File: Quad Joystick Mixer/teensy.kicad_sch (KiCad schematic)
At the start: 11 parts, among them U20 Teensy4.0

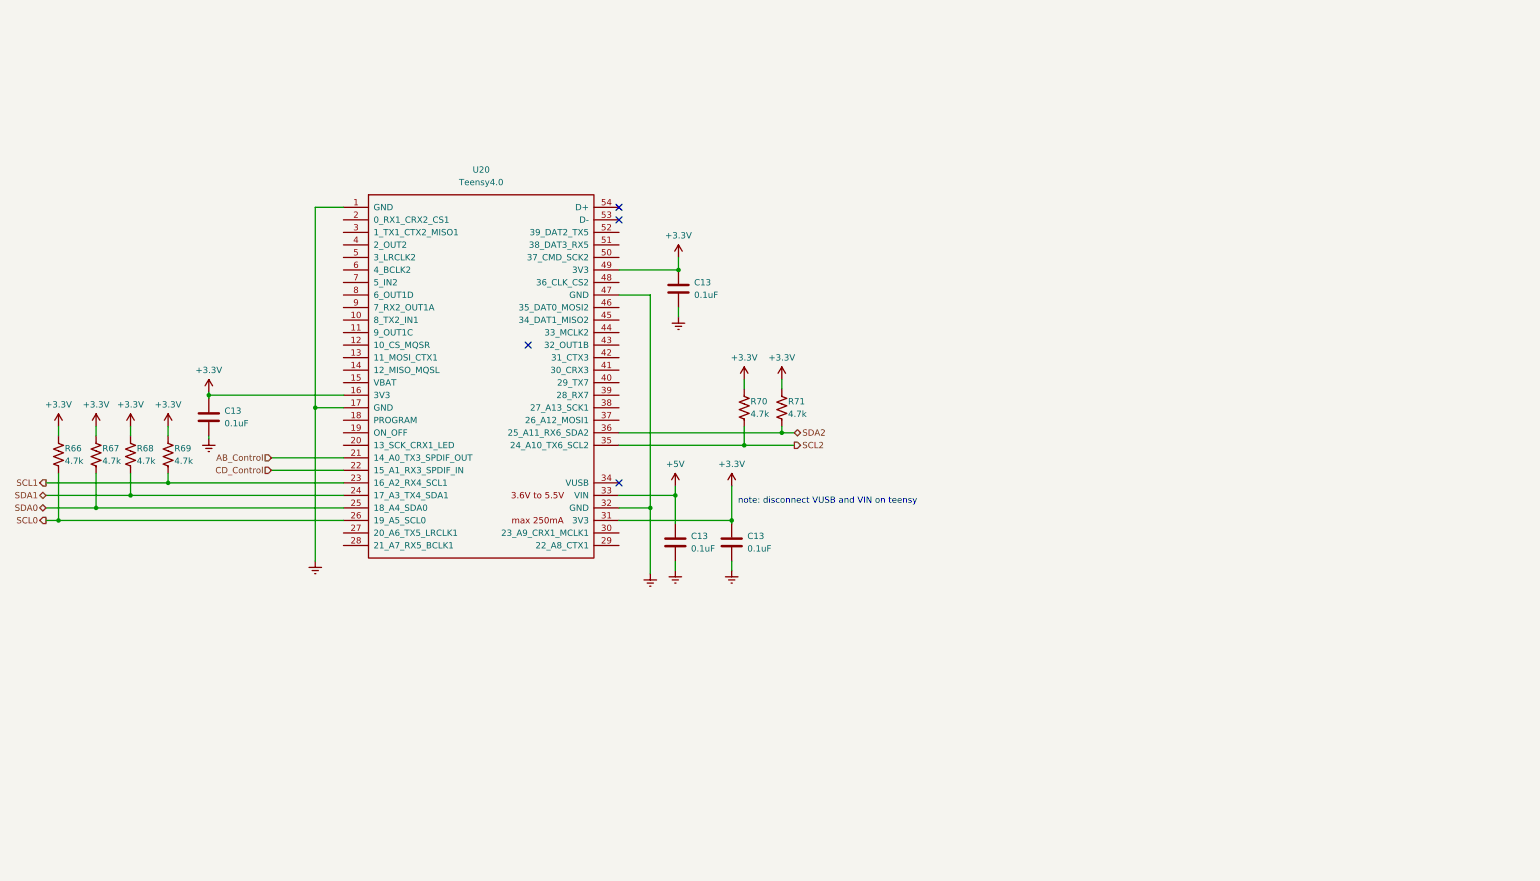
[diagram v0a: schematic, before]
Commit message: add in rotary circuit and some docs
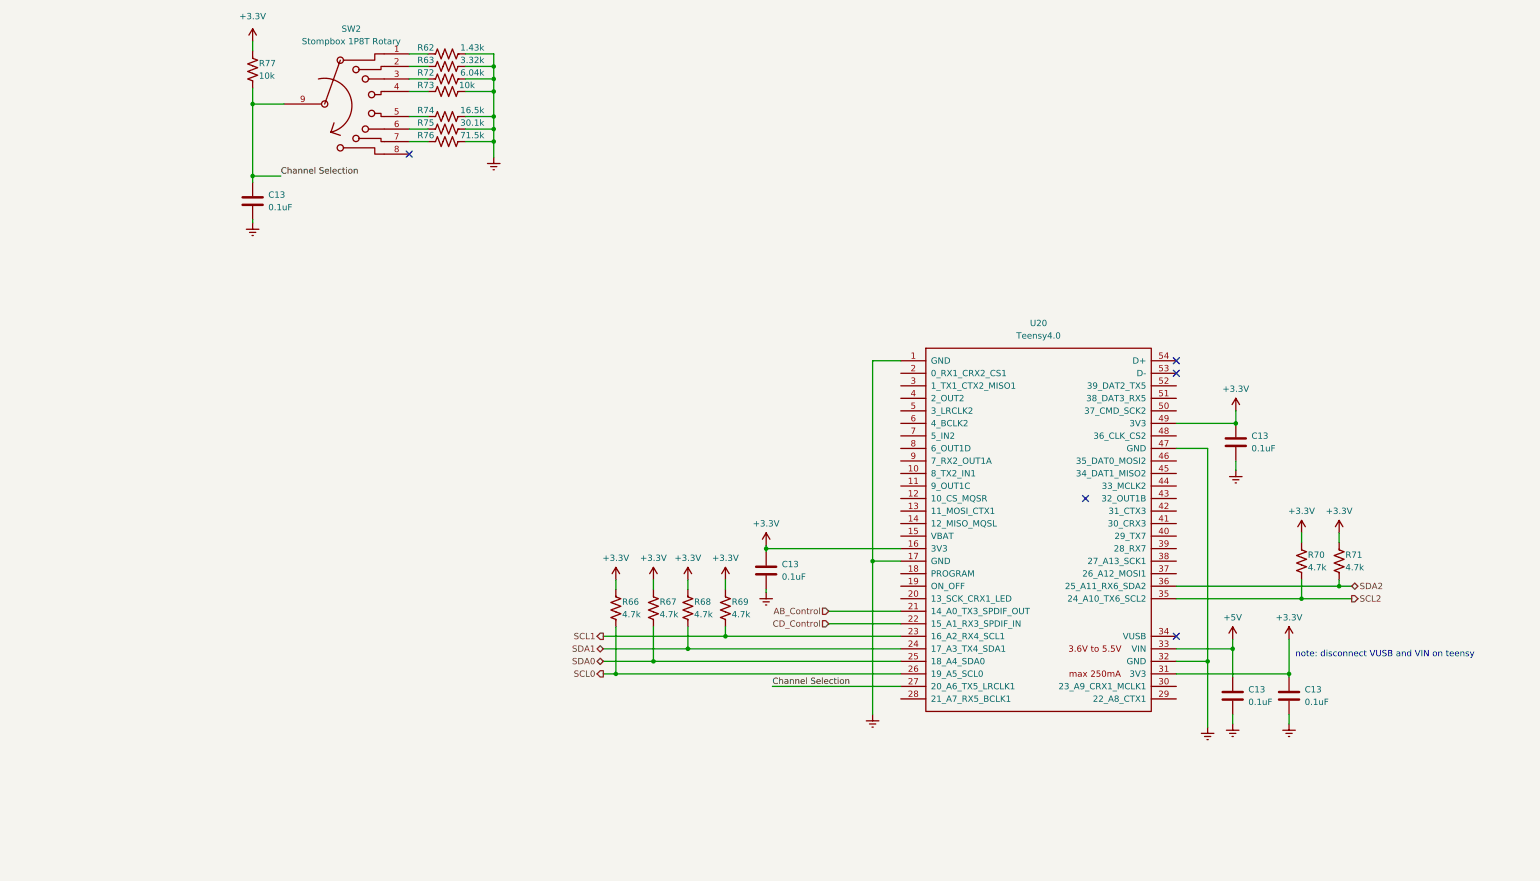
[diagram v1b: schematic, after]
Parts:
- added C13: 0.1uF, Capacitor_SMD:C_0805_2012Metric_Pad1.18x1.45mm_HandSolder, symbol Device:C
- added R62: 1.43k, symbol Device:R_US
- added R63: 3.32k, symbol Device:R_US
- added R72: 6.04k, symbol Device:R_US
- added R73, R77: 10k, symbol Device:R_US
- added R74: 16.5k, symbol Device:R_US
- added R75: 30.1k, symbol Device:R_US
- added R76: 71.5k, symbol Device:R_US
- added SW2: Stompbox 1P8T Rotary, Eyewool Switches:Stompbox 1P8T Rotary, symbol Eyewool_Switches:Stompbox 1P8T Rotary
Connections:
- net +3.3V: now also R77.1
- net Earth: now also C13.2, R62.2, R63.2, R72.2, R73.2, R74.2, R75.2, R76.2
- net Channel Selection: now reaches U20.27 (20_A6_TX5_LRCLK1)
- net Channel Selection: now also C13.1, R77.2, SW2.9
- new net: R63.1, SW2.2
- new net: R72.1, SW2.3
- new net: R62.1, SW2.1
- new net: R73.1, SW2.4
- new net: R74.1, SW2.5
- new net: R75.1, SW2.6
- new net: R76.1, SW2.7
- no-connect marks 4 -> 5
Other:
- moved on the sheet: C13, R66, R67, R68, R69, R70, R71, U20

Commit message: finished first draft of the schematic
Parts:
- removed C13: 0.1uF, Capacitor_SMD:C_0805_2012Metric_Pad1.18x1.45mm_HandSolder, symbol Device:C
- removed R62: 1.43k, symbol Device:R_US
- removed R63: 3.32k, symbol Device:R_US
- removed R72: 6.04k, symbol Device:R_US
- removed R73, R77: 10k, symbol Device:R_US
- removed R74: 16.5k, symbol Device:R_US
- removed R75: 30.1k, symbol Device:R_US
- removed R76: 71.5k, symbol Device:R_US
- removed SW2: Stompbox 1P8T Rotary, Eyewool Switches:Stompbox 1P8T Rotary, symbol Eyewool_Switches:Stompbox 1P8T Rotary
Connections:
- net Button_3: now reaches U20.10 (8_TX2_IN1)
- net LED_1: now reaches U20.4 (2_OUT2)
- net LED_2: now reaches U20.5 (3_LRCLK2)
- net Button_1: now reaches U20.8 (6_OUT1D)
- net Button_2: now reaches U20.9 (7_RX2_OUT1A)
- no-connect marks 5 -> 4
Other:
- note added: "Microcontroller"
- title: (none) -> Quadrophonic Joystick Mixer
- moved on the sheet: C13, R66, R67, R68, R69, R70, R71, U20

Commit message: ok the draft wasn't done but now i think it is
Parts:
- added C13 (x2): 0.1uF, Capacitor_SMD:C_0805_2012Metric_Pad1.18x1.45mm_HandSolder, symbol Device:C
- added D24 (x2): SMAJ3.3A, Diode_SMD:D_SMA, symbol Diode:SMAJ5.0A
- added SW5 (x2): ~, symbol Switch:SW_SPST
- added TP1: TestPoint, TestPoint:TestPoint_THTPad_D1.5mm_Drill0.7mm, symbol Connector:TestPoint
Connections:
- net +3.3V: now also TP1.1
- net Earth: now also C13.2, C13.2, D24.2 (A2), D24.2 (A2), SW5.2 (B), SW5.2 (B)
- net PROGRAM: now reaches U20.18 (PROGRAM)
- net PROGRAM: now also C13.1, D24.1 (A1), SW5.1 (A)
- net POWER: now reaches U20.19 (ON_OFF)
- net POWER: now also C13.1, D24.1 (A1), SW5.1 (A)
- no-connect marks 4 -> 29

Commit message: clean up after review, working through BOM
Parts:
- D24: value SMAJ3.3A -> SMAJ5.0A; DK PN (none) -> SMAJ5.0A-FDICT-ND; MPN (none) -> SMAJ5.0A-13-F
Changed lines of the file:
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@@
       (effects (font (size 1.27 1.27)) (justify left))
     )
-    (property "Value" "SMAJ3.3A" (at 199.39 191.135 90)
+    (property "Value" "SMAJ5.0A" (at 199.39 191.135 90)
       (effects (font (size 1.27 1.27)) (justify left))
     )
@@
     )
     (property "Datasheet" "https://www.littelfuse.com/media?resourcetype=datasheets&itemid=75e32973-b177-4ee3-a0ff-cedaf1abdb93&filename=smaj-datasheet" (at 196.85 188.595 0)
+      (effects (font (size 1.27 1.27)) hide)
+    )
+    (property "DK PN" "SMAJ5.0A-FDICT-ND" (at 196.85 189.865 0)
+      (effects (font (size 1.27 1.27)) hide)
+    )
+    (property "MPN" "SMAJ5.0A-13-F" (at 196.85 189.865 0)
       (effects (font (size 1.27 1.27)) hide)
     )
@@
       (effects (font (size 1.27 1.27)) (justify left))
     )
-    (property "Value" "SMAJ3.3A" (at 144.145 187.96 90)
+    (property "Value" "SMAJ5.0A" (at 144.145 187.96 90)
       (effects (font (size 1.27 1.27)) (justify left))
     )
@@
       (effects (font (size 1.27 1.27)) hide)
     )
+    (property "DK PN" "SMAJ5.0A-FDICT-ND" (at 141.605 186.69 0)
+      (effects (font (size 1.27 1.27)) hide)
+    )
+    (property "MPN" "SMAJ5.0A-13-F" (at 141.605 186.69 0)
+      (effects (font (size 1.27 1.27)) hide)
+    )

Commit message: finish adding parts to the BOM
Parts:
- C13, D24: Source (none) -> DK
- R66, R67, R68, R69, R70, R71: footprint (none) -> Resistor_SMD:R_0805_2012Metric_Pad1.20x1.40mm_HandSolder; DK PN (none) -> RMCF0805JT4K70CT-ND; MPN (none) -> RMCF0805JT4K70; Source (none) -> DK
- SW5: value ~ -> Cherry MX; footprint (none) -> Button_Switch_Keyboard:SW_Cherry_MX_1.00u_PCB; DK PN (none) -> CH160-ND; MPN (none) -> MX1A-11NW; Source (none) -> DK
- TP1: Source (none) -> NA
- U20: Source (none) -> Teensy
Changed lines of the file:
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@@
+      (effects (font (size 1.27 1.27)) hide)
+    )
+    (property "Source" "DK" (at 128.905 185.42 0)
       (effects (font (size 1.27 1.27)) hide)
     )
@@
     )
     (property "MPN" "CL21B104KBCNNNC" (at 248.92 114.935 0)
+      (effects (font (size 1.27 1.27)) hide)
+    )
+    (property "Source" "DK" (at 248.92 114.935 0)
       (effects (font (size 1.27 1.27)) hide)
     )
@@
       (effects (font (size 1.27 1.27)) hide)
     )
+    (property "Source" "DK" (at 259.715 166.37 0)
+      (effects (font (size 1.27 1.27)) hide)
+    )
     (pin "1")
     (pin "2")
@@
       (effects (font (size 1.27 1.27)) (justify left))
     )
-    (property "Footprint" "" (at 124.206 148.844 90)
+    (property "Footprint" "Resistor_SMD:R_0805_2012Metric_Pad1.20x1.40mm_HandSolder" (at 124.206 148.844 90)
       (effects (font (size 1.27 1.27)) hide)
     )
@@
       (effects (font (size 1.27 1.27)) hide)
     )
+    (property "Source" "DK" (at 123.19 148.59 0)
+      (effects (font (size 1.27 1.27)) hide)
+    )
+    (property "DK PN" "RMCF0805JT4K70CT-ND" (at 123.19 148.59 0)
+      (effects (font (size 1.27 1.27)) hide)
+    )
+    (property "MPN" "RMCF0805JT4K70" (at 123.19 148.59 0)
+      (effects (font (size 1.27 1.27)) hide)
+    )
     (pin "1")
     (pin "2")
@@
     )
     (property "MPN" "CL21B104KBCNNNC" (at 248.285 166.37 0)
+      (effects (font (size 1.27 1.27)) hide)
+    )
+    (property "Source" "DK" (at 248.285 166.37 0)
       (effects (font (size 1.27 1.27)) hide)
     )
@@
       (effects (font (size 1.27 1.27)) (justify left))
     )
-    (property "Footprint" "" (at 270.891 139.319 90)
+    (property "Footprint" "Resistor_SMD:R_0805_2012Metric_Pad1.20x1.40mm_HandSolder" (at 270.891 139.319 90)
       (effects (font (size 1.27 1.27)) hide)
     )
     (property "Datasheet" "~" (at 269.875 139.065 0)
+      (effects (font (size 1.27 1.27)) hide)
+    )
+    (property "Source" "DK" (at 269.875 139.065 0)
+      (effects (font (size 1.27 1.27)) hide)
+    )
+    (property "DK PN" "RMCF0805JT4K70CT-ND" (at 269.875 139.065 0)
+      (effects (font (size 1.27 1.27)) hide)
+    )
+    (property "MPN" "RMCF0805JT4K70" (at 269.875 139.065 0)
       (effects (font (size 1.27 1.27)) hide)
     )
@@
     )
     (property "Datasheet" "~" (at 266.7 165.1 0)
+      (effects (font (size 1.27 1.27)) hide)
+    )
+    (property "Source" "NA" (at 266.7 160.02 0)
       (effects (font (size 1.27 1.27)) hide)
     )
@@
       (effects (font (size 1.27 1.27)) (justify left))
     )
-    (property "Footprint" "" (at 138.811 148.844 90)
+    (property "Footprint" "Resistor_SMD:R_0805_2012Metric_Pad1.20x1.40mm_HandSolder" (at 138.811 148.844 90)
       (effects (font (size 1.27 1.27)) hide)
     )
@@
       (effects (font (size 1.27 1.27)) hide)
     )
+    (property "Source" "DK" (at 137.795 148.59 0)
+      (effects (font (size 1.27 1.27)) hide)
+    )
+    (property "DK PN" "RMCF0805JT4K70CT-ND" (at 137.795 148.59 0)
+      (effects (font (size 1.27 1.27)) hide)
+    )
+    (property "MPN" "RMCF0805JT4K70" (at 137.795 148.59 0)
+      (effects (font (size 1.27 1.27)) hide)
+    )
     (pin "1")
     (pin "2")
@@
     )
     (property "MPN" "CL21B104KBCNNNC" (at 153.67 140.97 0)
+      (effects (font (size 1.27 1.27)) hide)
+    )
+    (property "Source" "DK" (at 153.67 140.97 0)
       (effects (font (size 1.27 1.27)) hide)
     )
@@
       (effects (font (size 1.27 1.27)) (justify left))
     )
-    (property "Footprint" "" (at 146.431 148.844 90)
+    (property "Footprint" "Resistor_SMD:R_0805_2012Metric_Pad1.20x1.40mm_HandSolder" (at 146.431 148.844 90)
       (effects (font (size 1.27 1.27)) hide)
     )
     (property "Datasheet" "~" (at 145.415 148.59 0)
+      (effects (font (size 1.27 1.27)) hide)
+    )
+    (property "Source" "DK" (at 145.415 148.59 0)
+      (effects (font (size 1.27 1.27)) hide)
+    )
+    (property "DK PN" "RMCF0805JT4K70CT-ND" (at 145.415 148.59 0)
+      (effects (font (size 1.27 1.27)) hide)
+    )
+    (property "MPN" "RMCF0805JT4K70" (at 145.415 148.59 0)
       (effects (font (size 1.27 1.27)) hide)
     )
@@
       (effects (font (size 1.27 1.27)) (justify left))
     )
-    (property "Value" "~" (at 160.02 187.325 90)
-      (effects (font (size 1.27 1.27)) (justify left))
-    )
-    (property "Footprint" "" (at 157.48 186.055 0)
+    (property "Value" "Cherry MX" (at 160.02 187.325 90)
+      (effects (font (size 1.27 1.27)) (justify left))
+    )
+    (property "Footprint" "Button_Switch_Keyboard:SW_Cherry_MX_1.00u_PCB" (at 157.48 186.055 0)
       (effects (font (size 1.27 1.27)) hide)
     )
     (property "Datasheet" "~" (at 157.48 186.055 0)
+      (effects (font (size 1.27 1.27)) hide)
+    )
+    (property "Source" "DK" (at 157.48 186.055 0)
+      (effects (font (size 1.27 1.27)) hide)
+    )
+    (property "DK PN" "CH160-ND" (at 157.48 186.055 0)
+      (effects (font (size 1.27 1.27)) hide)
+    )
+    (property "MPN" "MX1A-11NW" (at 157.48 186.055 0)
       (effects (font (size 1.27 1.27)) hide)
     )
@@
     )
     (property "MPN" "CL21B104KBCNNNC" (at 184.15 188.595 0)
+      (effects (font (size 1.27 1.27)) hide)
+    )
+    (property "Source" "DK" (at 184.15 188.595 0)
       (effects (font (size 1.27 1.27)) hide)
     )
@@
       (effects (font (size 1.27 1.27)) (justify left))
     )
-    (property "Footprint" "" (at 263.271 139.319 90)
+    (property "Footprint" "Resistor_SMD:R_0805_2012Metric_Pad1.20x1.40mm_HandSolder" (at 263.271 139.319 90)
       (effects (font (size 1.27 1.27)) hide)
     )
     (property "Datasheet" "~" (at 262.255 139.065 0)
+      (effects (font (size 1.27 1.27)) hide)
+    )
+    (property "Source" "DK" (at 262.255 139.065 0)
+      (effects (font (size 1.27 1.27)) hide)
+    )
+    (property "DK PN" "RMCF0805JT4K70CT-ND" (at 262.255 139.065 0)
+      (effects (font (size 1.27 1.27)) hide)
+    )
+    (property "MPN" "RMCF0805JT4K70" (at 262.255 139.065 0)
       (effects (font (size 1.27 1.27)) hide)
     )
@@
       (effects (font (size 1.27 1.27)) hide)
     )
+    (property "Source" "DK" (at 196.85 189.865 0)
+      (effects (font (size 1.27 1.27)) hide)
+    )
     (pin "1")
     (pin "2")
@@
     )
     (property "Datasheet" "" (at 198.755 127.635 0)
+      (effects (font (size 1.27 1.27)) hide)
+    )
+    (property "Source" "Teensy" (at 208.915 132.715 0)
       (effects (font (size 1.27 1.27)) hide)
     )
@@
       (effects (font (size 1.27 1.27)) (justify left))
     )
-    (property "Value" "~" (at 215.265 190.5 90)
-      (effects (font (size 1.27 1.27)) (justify left))
-    )
-    (property "Footprint" "" (at 212.725 189.23 0)
+    (property "Value" "Cherry MX" (at 215.265 190.5 90)
+      (effects (font (size 1.27 1.27)) (justify left))
+    )
+    (property "Footprint" "Button_Switch_Keyboard:SW_Cherry_MX_1.00u_PCB" (at 212.725 189.23 0)
       (effects (font (size 1.27 1.27)) hide)
     )
     (property "Datasheet" "~" (at 212.725 189.23 0)
+      (effects (font (size 1.27 1.27)) hide)
+    )
+    (property "Source" "DK" (at 212.725 189.23 0)
+      (effects (font (size 1.27 1.27)) hide)
+    )
+    (property "DK PN" "CH160-ND" (at 212.725 189.23 0)
+      (effects (font (size 1.27 1.27)) hide)
+    )
+    (property "MPN" "MX1A-11NW" (at 212.725 189.23 0)
       (effects (font (size 1.27 1.27)) hide)
     )
@@
     )
     (property "MPN" "SMAJ5.0A-13-F" (at 141.605 186.69 0)
+      (effects (font (size 1.27 1.27)) hide)
+    )
+    (property "Source" "DK" (at 141.605 186.69 0)
       (effects (font (size 1.27 1.27)) hide)
     )
@@
       (effects (font (size 1.27 1.27)) (justify left))
     )
-    (property "Footprint" "" (at 131.826 148.844 90)
+    (property "Footprint" "Resistor_SMD:R_0805_2012Metric_Pad1.20x1.40mm_HandSolder" (at 131.826 148.844 90)
       (effects (font (size 1.27 1.27)) hide)
     )
@@
       (effects (font (size 1.27 1.27)) hide)
     )
+    (property "Source" "DK" (at 130.81 148.59 0)
+      (effects (font (size 1.27 1.27)) hide)
+    )
+    (property "DK PN" "RMCF0805JT4K70CT-ND" (at 130.81 148.59 0)
+      (effects (font (size 1.27 1.27)) hide)
+    )
+    (property "MPN" "RMCF0805JT4K70" (at 130.81 148.59 0)
+      (effects (font (size 1.27 1.27)) hide)
+    )

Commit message: work on placement and layout
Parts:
- removed C13: 0.1uF, Capacitor_SMD:C_0805_2012Metric_Pad1.18x1.45mm_HandSolder, symbol Device:C
- removed R70, R71: 4.7k, Resistor_SMD:R_0805_2012Metric_Pad1.20x1.40mm_HandSolder, symbol Device:R_US
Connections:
- net +3.3V: no longer U20.49 (3V3)
- net Earth: no longer U20.47 (GND)
- net SCL2: no longer names the net of U20.35 (24_A10_TX6_SCL2)
- net SDA2: no longer names the net of U20.36 (25_A11_RX6_SDA2)
- no-connect marks 29 -> 34

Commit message: more progress on layout
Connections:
- net AB_Control: now also U20.22 (15_A1_RX3_SPDIF_IN); no longer U20.21 (14_A0_TX3_SPDIF_OUT)
- net CD_Control: now also U20.27 (20_A6_TX5_LRCLK1); no longer U20.22 (15_A1_RX3_SPDIF_IN)
- net Channel Selection: now also U20.21 (14_A0_TX3_SPDIF_OUT); no longer U20.27 (20_A6_TX5_LRCLK1)
- no-connect marks 34 -> 35
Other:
- moved on the sheet: R66, R67, R68, R69
